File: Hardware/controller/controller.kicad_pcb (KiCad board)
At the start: 4 copper layers, 128.1 x 184.5 mm, 118 parts, among them J101 Conn_02x10_Odd_Even, J102 Conn_02x10_Odd_Even, J103 Conn_02x10_Odd_Even, J104 Conn_02x08_Odd_Even, J301 Conn_ARM_JTAG_SWD_10, M101 Fan_4pin, Q101 MMBT3904, Q301 MMBT3904, SW301 B3F-1005, SW302 B3F-1002, SW303 228ADS2AAWFCMBA, U101 PCA9543A, U102 EMC2101-R, U201 BD9C301FJ, U302 ATSAME51J20A-A, U303 AT25SF321B-SSHB, U401 KSZ8041TL, X401 50MHz, Y302 12MHz

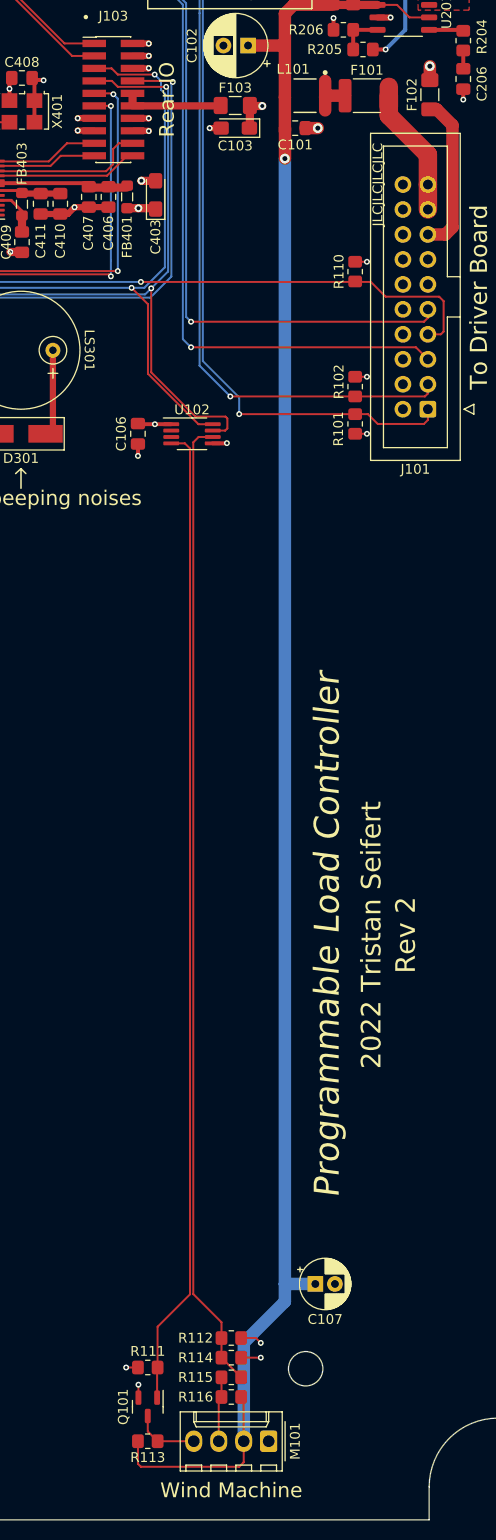
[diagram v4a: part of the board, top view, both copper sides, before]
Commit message: More controller board stuff
- Fixed the fan connector (to accomodate the physical/mechanical hole
  for the connector)

- Tweaked some more footprints to make them easier to solder
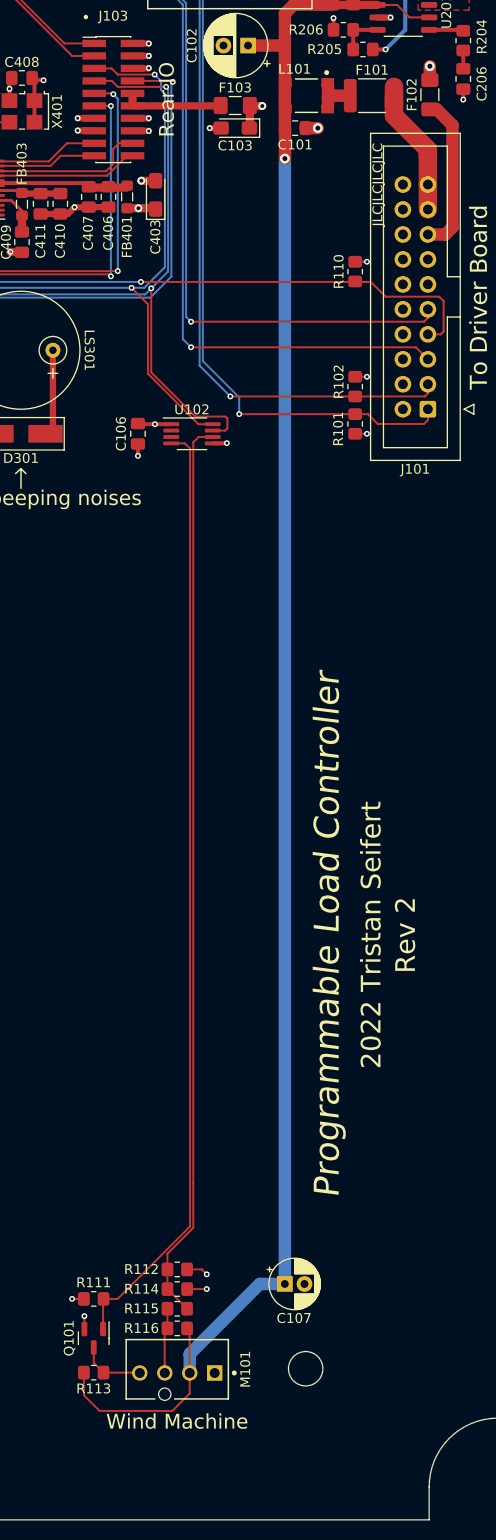
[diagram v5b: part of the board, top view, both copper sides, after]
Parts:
- M101: footprint Connector_Molex:Molex_KK-254_AE-6410-04A_1x04_P2.54mm_Vertical -> programmable-load:Molex-47053-1000-MFG
- moved M101 11.8 mm to (115.5, 189.2), turned to 0 degrees
- moved Q101 8.89 mm to (107.0, 186.0)
- moved R111 8.89 mm to (107.0, 182.0)
- moved R112 8.89 mm to (115.5, 179.0)
- moved R113 8.89 mm to (107.0, 189.5)
- moved R114 8.89 mm to (115.5, 181.0)
- moved R115 8.89 mm to (115.5, 183.0)
- moved R116 8.89 mm to (115.5, 185.0)
- moved C107 3.10 mm to (126.4, 180.5)
- moved F101 0.52 mm to (135.3, 59.6)
- moved L101 0.15 mm to (128.7, 59.6)
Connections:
- U302 pad 16: /CPU/FAN_PWM -> unconnected-(U302-Pad16)
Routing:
- net /FAN_TACH: track 99.4 -> 92.3 mm
- net +12V: track 192.2 -> 187.1 mm
- net /FAN_PWM: track 100.1 -> 96.2 mm
- net Net-(F101-Pad2): track 5.09 -> 4.34 mm

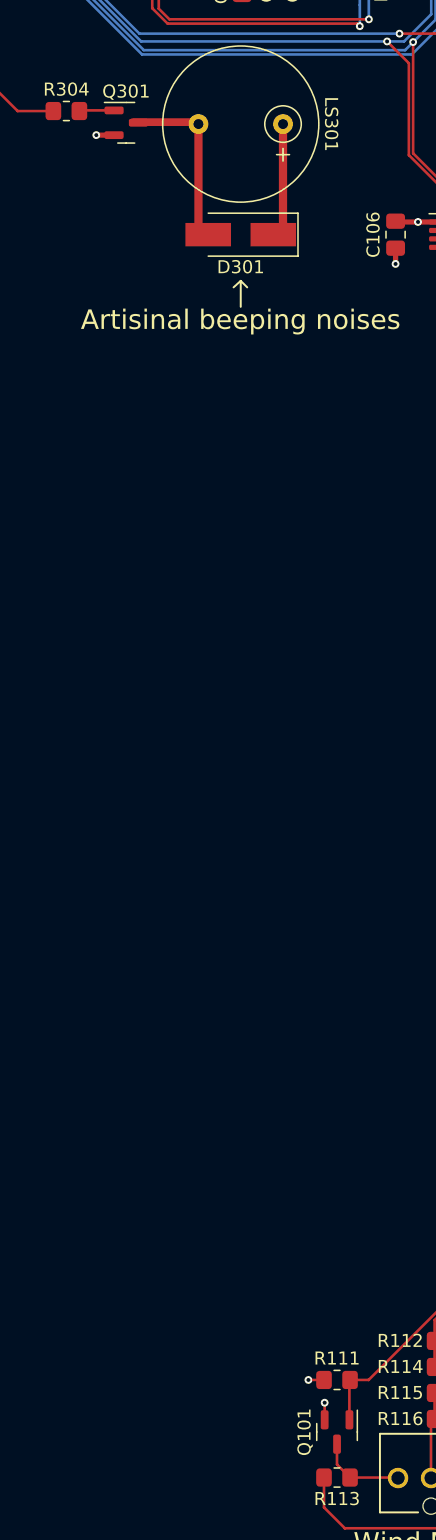
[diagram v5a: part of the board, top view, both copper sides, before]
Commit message: Final bits of tweaks for rev2 analog board
- Fixed footprint of MMBT3904 transistors on driver and controller
  boards (it is SOT-323, not SC-70)

- A few more minor modifications to the layout of the analog driver
  board for rev2
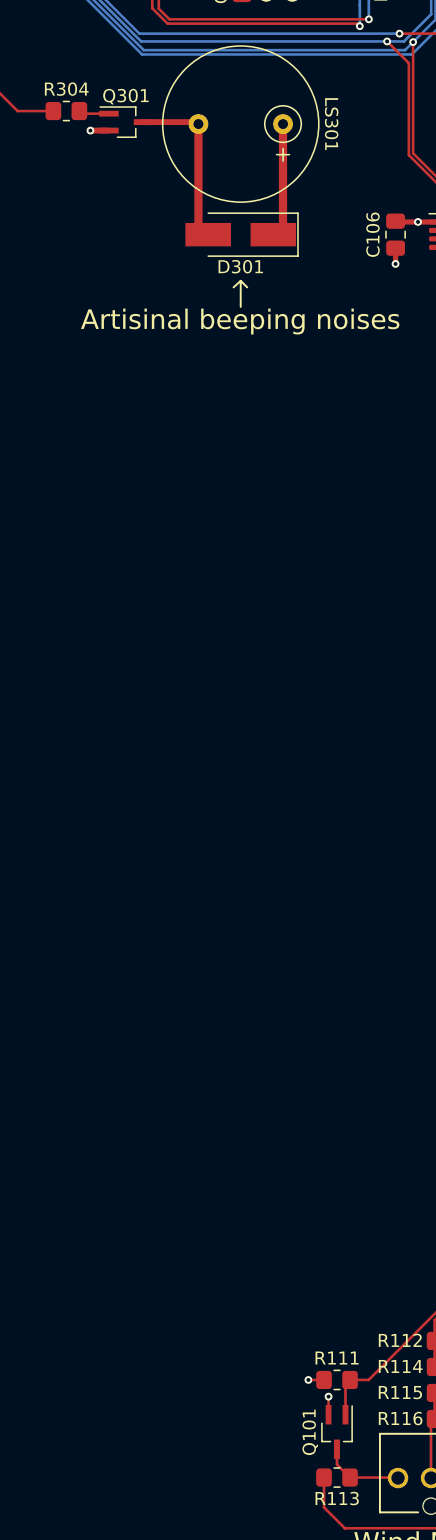
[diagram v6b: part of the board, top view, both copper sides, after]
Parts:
- Q101, Q301: footprint Package_TO_SOT_SMD:SOT-23 -> Package_TO_SOT_SMD:SOT-323_SC-70_Handsoldering
- moved Q301 0.05 mm to (90.8, 85.3)
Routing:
- net Net-(D301-Pad2): track 13.8 -> 13.1 mm

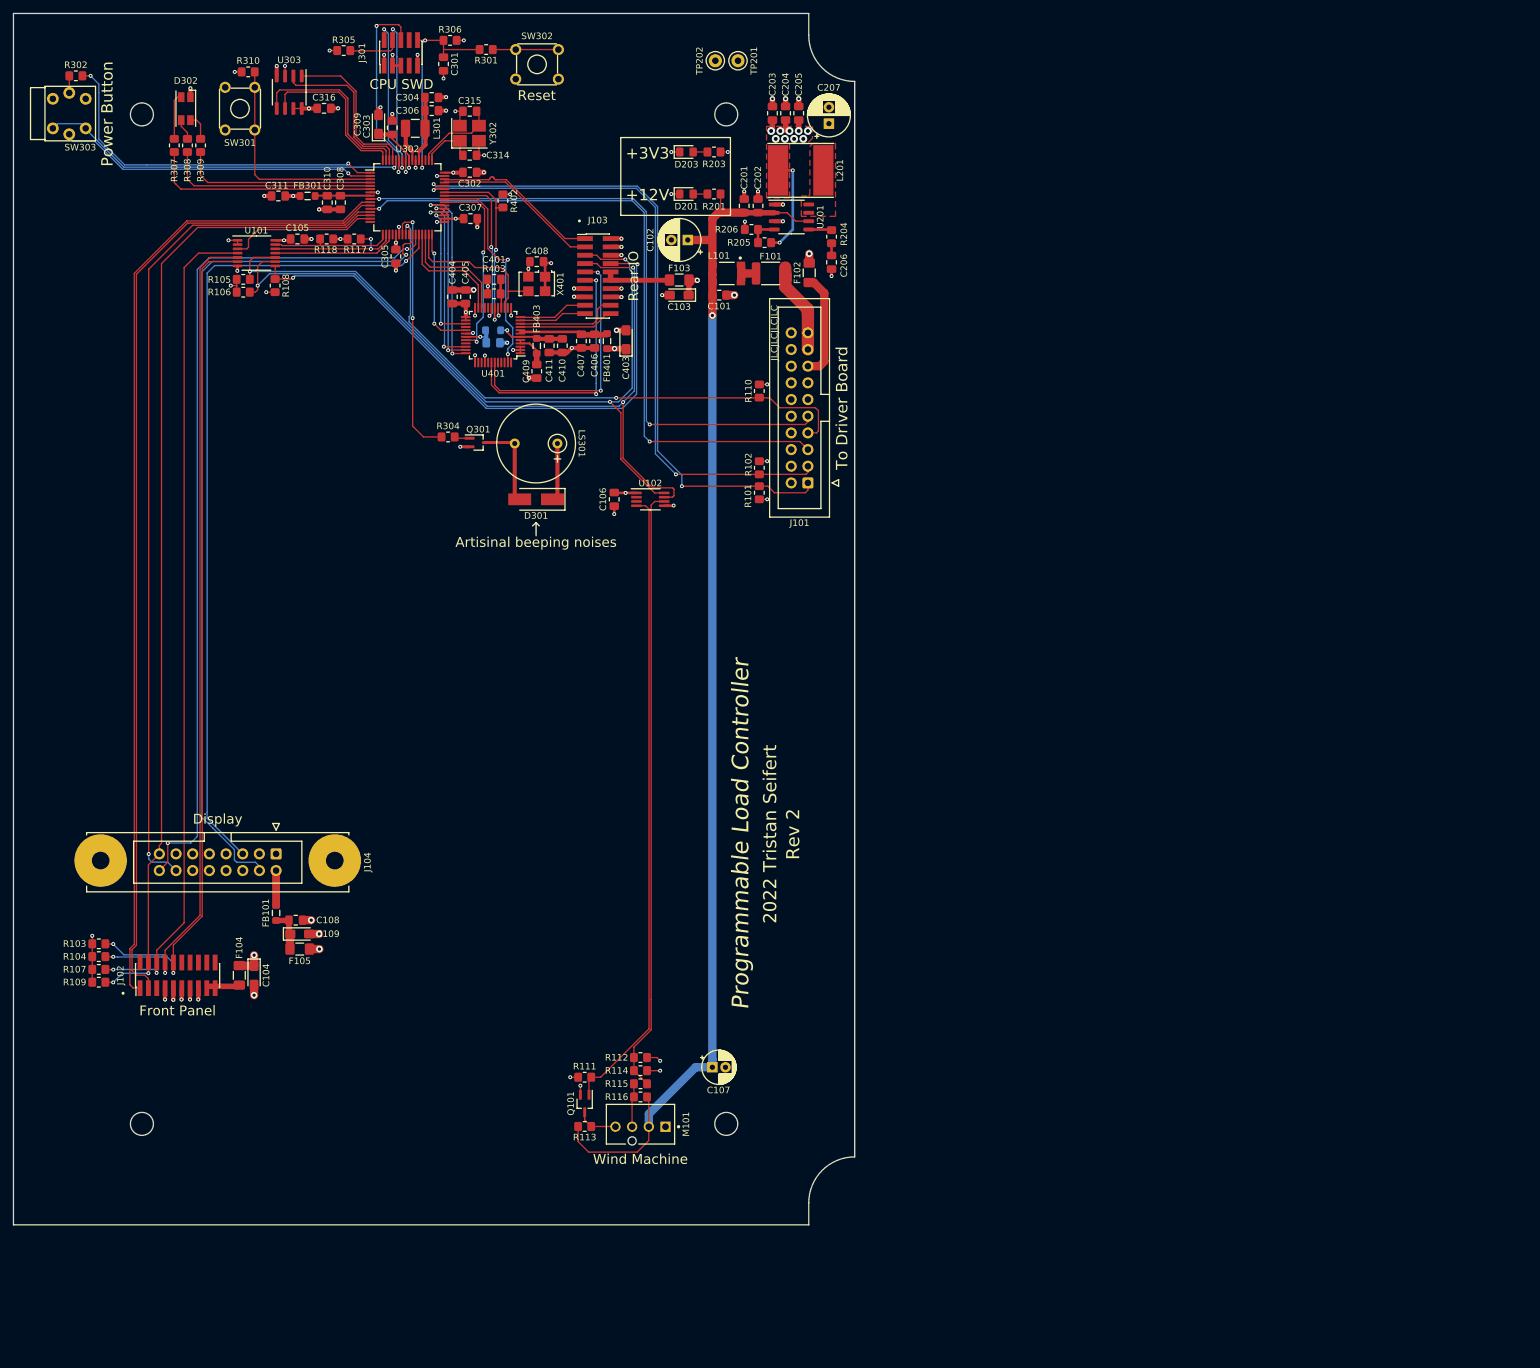
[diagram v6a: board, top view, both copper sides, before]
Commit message: Start work on rev3 hardware
- This fits the Technomet R110 enclosure and supports multiple load
  boards, connected via CAN rather than I2C. Each load has a
  microcontroller of its own.
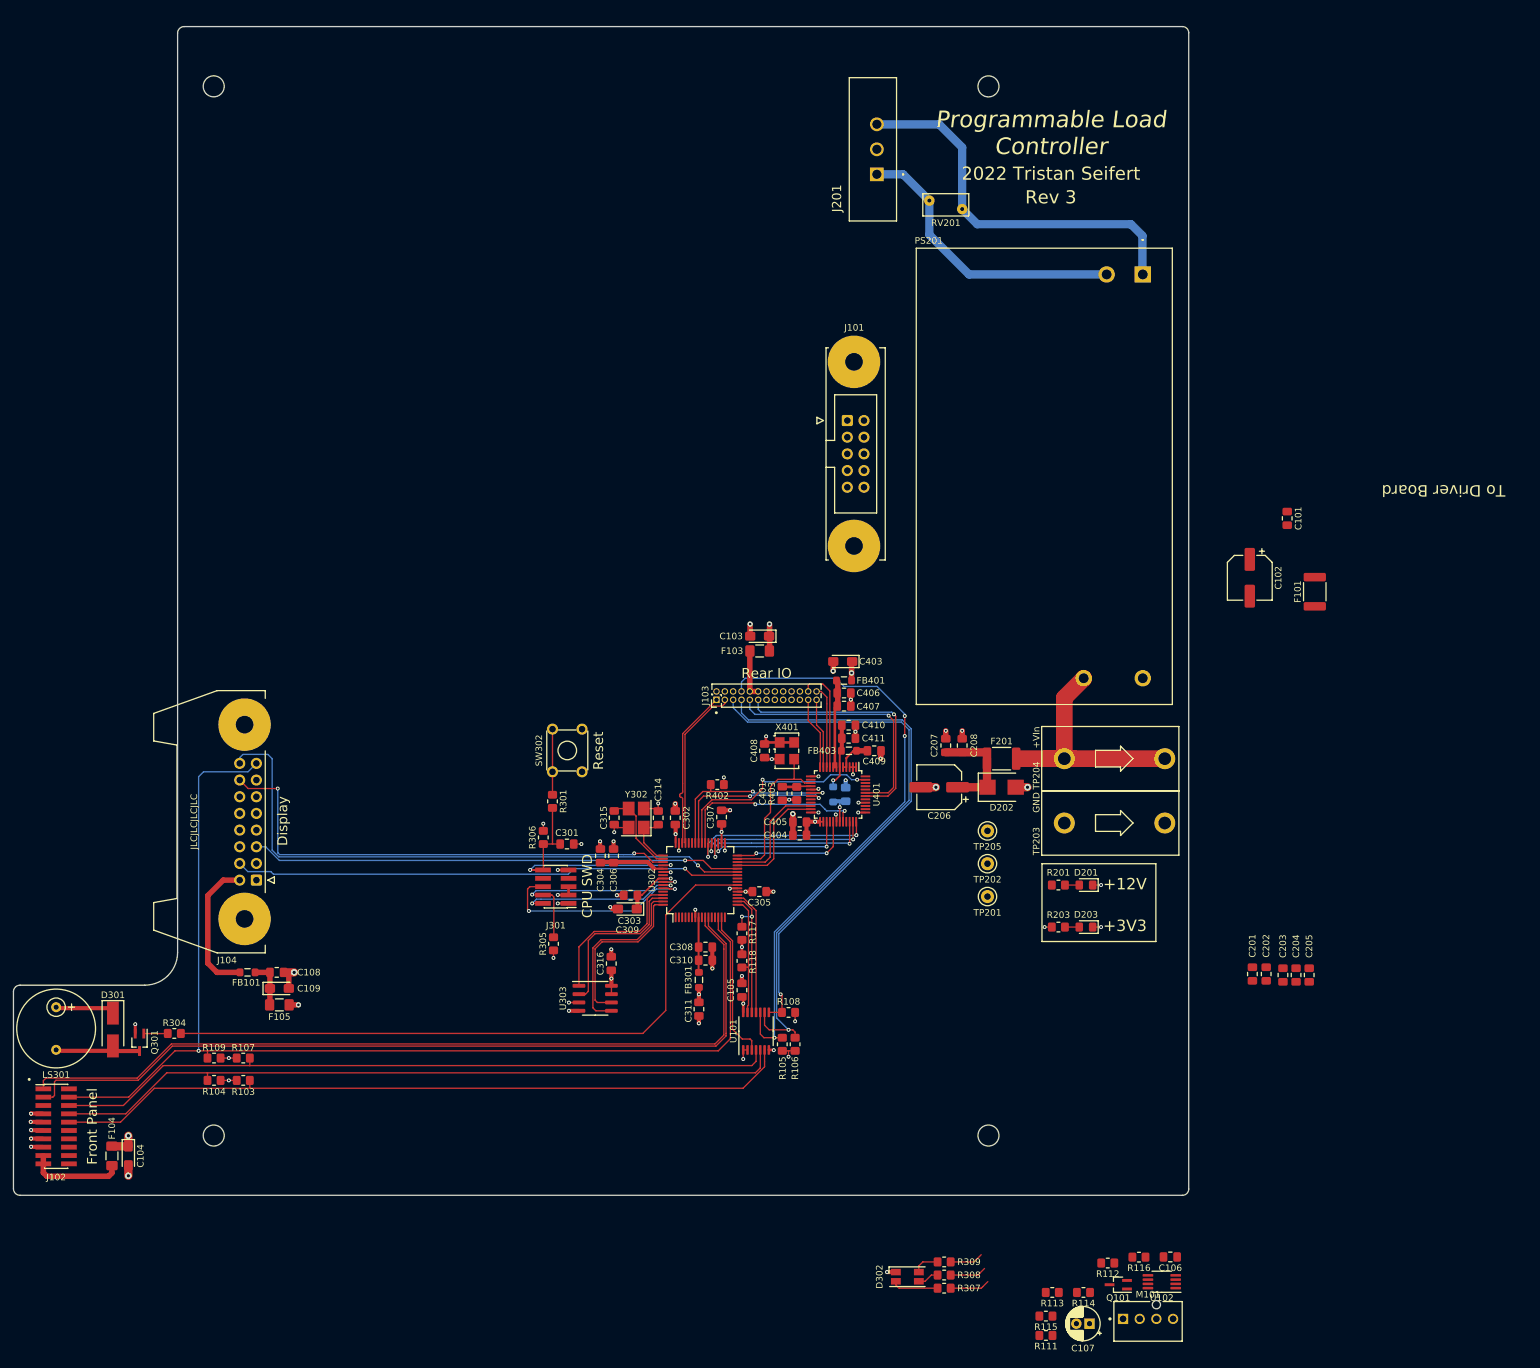
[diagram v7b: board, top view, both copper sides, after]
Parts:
- removed F102: 250mA, Fuse:Fuse_1206_3216Metric_Pad1.42x1.75mm_HandSolder
- removed L101: Choke, programmable-load:Bourns-SRF4532-0-0-MFG
- removed L201: 4.7µH, Inductor_SMD:L_Taiyo-Yuden_NR-80xx_HandSoldering
- removed L301: 10µH, Inductor_SMD:L_1210_3225Metric_Pad1.42x2.65mm_HandSolder
- removed R101, R102: 2k2, Resistor_SMD:R_0805_2012Metric_Pad1.20x1.40mm_HandSolder
- removed R110, R310: 10k, Resistor_SMD:R_0805_2012Metric_Pad1.20x1.40mm_HandSolder
- removed R204: 12k, Resistor_SMD:R_0805_2012Metric_Pad1.20x1.40mm_HandSolder
- removed R205: 7k5, Resistor_SMD:R_0805_2012Metric_Pad1.20x1.40mm_HandSolder
- removed R206: 2k4, Resistor_SMD:R_0805_2012Metric_Pad1.20x1.40mm_HandSolder
- removed R302: 330R, Resistor_SMD:R_0805_2012Metric_Pad1.20x1.40mm_HandSolder
- removed SW301: B3F-1005, Button_Switch_THT:SW_TH_Tactile_Omron_B3F-10xx
- removed SW303: 228ADS2AAWFCMBA, programmable-load:CTS-228ADS2
- removed U201: BD9C301FJ, Package_SO:SOP-8_3.9x4.9mm_P1.27mm
- added C208: 1µF, Capacitor_SMD:C_0805_2012Metric_Pad1.18x1.45mm_HandSolder, F.Cu at (164.5, 131.5)
- added D202: SM6T22A, Diode_SMD:D_SMB, F.Cu at (170.5, 137.8)
- added F201: 2A, Fuse:Fuse_1812_4532Metric_Pad1.30x3.40mm_HandSolder, F.Cu at (170.5, 133.5)
- added J201: Screw_Terminal_01x03, programmable-load:CUI_TBP02R2W-381-03BE, F.Cu at (151.5, 44.5)
- added PS201: PSK-30D-12, programmable-load:CONV_PSK-30D-12, F.Cu at (177.0, 90.5)
- added RV201: Varistor, Varistor:RV_Disc_D7mm_W3.4mm_P5mm, F.Cu at (164.5, 49.8)
- added TP203: TestPoint, programmable-load:DELTRON-571-0x00, F.Cu at (197.5, 143.3)
- added TP204: TestPoint, programmable-load:DELTRON-571-0x00, F.Cu at (197.5, 133.5)
- added TP205: +12V, TestPoint:TestPoint_Keystone_5000-5004_Miniature, F.Cu at (168.3, 144.5)
- C102: footprint Capacitor_THT:CP_Radial_D6.3mm_P2.50mm -> Capacitor_SMD:CP_Elec_6.3x5.4
- C206: value 4700pF -> 47µF; footprint Capacitor_SMD:C_0805_2012Metric_Pad1.18x1.45mm_HandSolder -> Capacitor_SMD:CP_Elec_6.3x5.4
- C207: value 68µF -> 10µF; footprint Capacitor_THT:CP_Radial_D6.3mm_P2.50mm -> Capacitor_SMD:C_0805_2012Metric_Pad1.18x1.45mm_HandSolder
- F101: value 1A -> 1.6A
- H101, H102, H103, H104: footprint MountingHole:MountingHole_3.5mm -> MountingHole:MountingHole_3.2mm_M3
- J101: footprint Connector_IDC:IDC-Header_2x10_P2.54mm_Vertical -> Connector_IDC:IDC-Header_2x05-1MP_P2.54mm_Latch_Vertical
- J103: footprint Connector_PinHeader_1.27mm:PinHeader_2x10_P1.27mm_Vertical_SMD -> Connector_PinHeader_1.27mm:PinHeader_2x13_P1.27mm_Vertical
- J104: footprint Connector_IDC:IDC-Header_2x08-1MP_P2.54mm_Latch_Vertical -> Connector_IDC:IDC-Header_2x08-1MP_P2.54mm_Latch_Horizontal
- moved R307 209.9 mm to (161.8, 214.2), turned to 0 degrees
- moved D302 209.1 mm to (156.2, 212.4), turned to 0 degrees
- moved R308 207.1 mm to (161.8, 212.2), turned to 0 degrees
- moved R309 204.3 mm to (161.8, 210.2), turned to 0 degrees
- moved C203 152.6 mm to (213.3, 166.4)
- moved C204 152.6 mm to (215.3, 166.4)
- moved C205 152.6 mm to (217.3, 166.4)
- moved U303 145.7 mm to (108.6, 170.0), turned to 0 degrees
- moved C106 143.1 mm to (196.2, 209.4), turned to 180 degrees
- moved R105 142.5 mm to (137.1, 177.0), turned to -90 degrees
- moved U102 142.4 mm to (194.9, 213.2), turned to 180 degrees
- moved R106 142.1 mm to (139.1, 177.0), turned to -90 degrees
- moved U101 140.8 mm to (133.1, 175.0), turned to 90 degrees
- moved C202 140.3 mm to (210.8, 166.3)
- moved C201 140.3 mm to (208.7, 166.3)
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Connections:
- C206 pad 1: GND -> +12V
- C206 pad 2: Net-(C206-Pad2) -> GND
- C207 pad 1: +3V3 -> GND
- C207 pad 2: GND -> +12V
- F101 pad 2: Net-(F101-Pad2) -> +12V
- J101 pad 1: /EXT_SCL -> unconnected-(J101-Pad1)
- J101 pad 10: GND -> Net-(J101-Pad10)
- J101 pad 2: GND -> Net-(J101-Pad10)
- J101 pad 3: /EXT_SDA -> unconnected-(J101-Pad3)
- J101 pad 4: GND -> Net-(J101-Pad10)
- J101 pad 5: /~{EXT_IRQ} -> Net-(F101-Pad1)
- J101 pad 6: GND -> Net-(J101-Pad10)
- J101 pad 7: /~{EXT_TRIG} -> Net-(F101-Pad1)
- J101 pad 8: GND -> Net-(J101-Pad10)
- J101 pad 9: /~{EXT_RESET} -> Net-(F101-Pad1)
- J103 pad 17: /ETH_TX- -> unconnected-(J103-Pad17)
- J103 pad 18: /ETH_RX+ -> /CAN-
- J103 pad 19: /ETH_TX+ -> unconnected-(J103-Pad19)
- J103 pad 20: /ETH_RX- -> /CAN+
- J103 pad 5: /IO_SCL -> /IO_SDA
- J103 pad 7: /IO_SDA -> /~{IO_IRQ}
- J103 pad 8: /~{IO_IRQ} -> /IO_SCL
- U302 pad 1: /CPU/PWRLED1 -> unconnected-(U302-Pad1)
- U302 pad 12: /~{EXT_IRQ} -> unconnected-(U302-Pad12)
- U302 pad 13: /DISP_D/~{C} -> unconnected-(U302-Pad13)
- U302 pad 2: /CPU/PWRLED0 -> unconnected-(U302-Pad2)
- U302 pad 24: /~{EXT_TRIG} -> /~{TRIGGER}
- U302 pad 3: /CPU/MODE -> unconnected-(U302-Pad3)
- U302 pad 43: /EXT_SDA -> /CPU/CAN_TX
- U302 pad 44: /EXT_SCL -> /CPU/CAN_RX
- U302 pad 51: unconnected-(U302-Pad51) -> /DISP_D/~{C}
- U302 pad 55: Net-(L301-Pad1) -> unconnected-(U302-Pad55)
- U302 pad 60: /CPU/PWRBTN -> unconnected-(U302-Pad60)
- U302 pad 9: /~{EXT_RESET} -> unconnected-(U302-Pad9)
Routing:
- net +12V: track 187.1 -> 14.7 mm, vias 1 -> 0
- net /~{EXT_IRQ}: track 102.8 -> 0.00 mm, vias 2 -> 0
- net /EXT_SCL: track 102.3 -> 0.00 mm, vias 2 -> 0
- net /~{EXT_RESET}: track 100.6 -> 0.00 mm, vias 2 -> 0
- net /EXT_SDA: track 99.9 -> 0.00 mm, vias 2 -> 0
- net /FAN_PWM: track 95.9 -> 0.00 mm
- net /FAN_TACH: track 92.3 -> 0.00 mm
- net /~{EXT_TRIG}: track 89.1 -> 0.00 mm, vias 2 -> 0
- net /CPU/BEEPER: track 39.4 -> 102.6 mm, vias 2 -> 0
- net LINE: track 0.00 -> 58.9 mm
- net /DISP_D/~{C}: track 132.1 -> 75.5 mm, vias 1 -> 2
- net /CPU/PWRBTN: track 56.4 -> 0.00 mm, vias 1 -> 0
- net /DISP_SCK: track 133.2 -> 77.2 mm
- net /CPU/PWRLED1: track 55.0 -> 0.00 mm, vias 2 -> 0
- net /DISP_MOSI: track 126.6 -> 74.6 mm
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- removed copper zone on F.Cu, net +3V3
- removed copper zone on F.Cu, net Net-(L201-Pad1)
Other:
- board size 128.1 x 184.5 mm -> 179 x 178 mm
- board text added: "+VIn"
- board text added: "GND"
- board text added: "Rev 3"
- board text removed: "Artisinal beeping noises"
- board text removed: "Power Button"
- board text removed: "Rev 2"
- board text removed: "Wind Machine"
